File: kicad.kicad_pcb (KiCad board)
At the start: 2 copper layers, 0 parts

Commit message: demasiados cambios mi loco
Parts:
- added C1: 100nF, Capacitor_SMD:C_1206_3216Metric_Pad1.33x1.80mm_HandSolder, F.Cu at (121.9, 113.0)
- added C10: 470uF, libs:CAP_10x10_SMD_THT, F.Cu at (116.8, 88.4)
- added C11: 470uF, libs:CAP_10x10_SMD_THT, F.Cu at (133.8, 64.2)
- added C12: 470uF, libs:CAP_10x10_SMD_THT, F.Cu at (116.8, 76.6)
- added C18: 100nF, Capacitor_SMD:C_1206_3216Metric_Pad1.33x1.80mm_HandSolder, F.Cu at (166.3, 102.7)
- added C19: 100nF, Capacitor_SMD:C_1206_3216Metric_Pad1.33x1.80mm_HandSolder, F.Cu at (166.3, 99.3)
- added C22: 1uF, Capacitor_SMD:C_1206_3216Metric_Pad1.33x1.80mm_HandSolder, F.Cu at (107.8, 126.0)
- added C5: 470uF, libs:CAP_10x10_SMD_THT, F.Cu at (130.9, 87.9)
- added C6: 470uF, libs:CAP_10x10_SMD_THT, F.Cu at (119.8, 64.2)
- added C7: 100nF, Capacitor_SMD:C_1206_3216Metric_Pad1.33x1.80mm_HandSolder, F.Cu at (140.7, 84.6)
- added C8: 470uF, libs:CAP_10x10_SMD_THT, F.Cu at (147.9, 64.2)
- added C9: 470uF, libs:CAP_10x10_SMD_THT, F.Cu at (130.9, 76.1)
- added D15: BAT54S, Package_TO_SOT_SMD:SOT-23, F.Cu at (205.4, 60.6)
- added D2: SS14, Diode_SMD:D_SMA_Handsoldering, F.Cu at (99.8, 126.7)
- added D5: LED, LED_SMD:LED_1206_3216Metric, F.Cu at (186.4, 64.5)
- added D6: LED, LED_SMD:LED_1206_3216Metric, F.Cu at (150.4, 78.3)
- added D7: SS14, Diode_SMD:D_SMA_Handsoldering, F.Cu at (142.7, 72.4)
- added D8: M7, Diode_SMD:D_SMA_Handsoldering, F.Cu at (188.6, 60.6)
- added D9: BAT54S, Package_TO_SOT_SMD:SOT-23, F.Cu at (170.2, 81.7)
- added J1: Screw_Terminal_01x02, libs:TerminalBlock_bornier-2_P5.08mm, F.Cu at (138.8, 102.2)
- added J2: Screw_Terminal_01x03, libs:TerminalBlock_bornier-3_P5.08mm, F.Cu at (122.2, 102.2)
- added J3: ICSP, Connector_PinSocket_2.54mm:PinSocket_1x06_P2.54mm_Vertical, F.Cu at (116.6, 100.0)
- added J4: Conn_01x05, Connector_Molex:Molex_KK-254_AE-6410-05A_1x05_P2.54mm_Vertical, F.Cu at (116.6, 118.9)
- added J7: Conn_01x03, Connector_Molex:Molex_KK-254_AE-6410-03A_1x03_P2.54mm_Vertical, F.Cu at (155.9, 101.6)
- added JP1: SolderJumper_2_Open, Jumper:SolderJumper-2_P1.3mm_Open_RoundedPad1.0x1.5mm, F.Cu at (156.9, 60.1)
- added K1: RELAY, Relay_THT:Relay_SPDT_SANYOU_SRD_Series_Form_C, F.Cu at (164.5, 66.8)
- added L1: 68uH, libs:L_12x12mm_H8mm, F.Cu at (102.2, 77.8)
- added Q1: BC817, Package_TO_SOT_SMD:SOT-23, F.Cu at (191.4, 65.1)
- added R1: 10k, Resistor_SMD:R_1206_3216Metric, F.Cu at (142.4, 118.2)
- added R11: 10k, Resistor_SMD:R_1206_3216Metric, F.Cu at (142.4, 111.6)
- added R12: 10k, Resistor_SMD:R_1206_3216Metric, F.Cu at (129.7, 125.5)
- added R15: 10k, Resistor_SMD:R_1206_3216Metric, F.Cu at (142.4, 108.3)
- added R16: 1k, Resistor_SMD:R_1206_3216Metric, F.Cu at (103.2, 93.0)
- added R17: 330, Resistor_SMD:R_1206_3216Metric, F.Cu at (97.6, 93.0)
- added R18: 1k, Resistor_SMD:R_1206_3216Metric, F.Cu at (165.2, 84.3)
- added R19: 1k, Resistor_SMD:R_1206_3216Metric, F.Cu at (165.2, 81.0)
- added R2: 10k, Resistor_SMD:R_1206_3216Metric, F.Cu at (135.3, 125.5)
- added R20: 10k, Resistor_SMD:R_1206_3216Metric, F.Cu at (142.4, 121.5)
- added R23: 1k, Resistor_SMD:R_1206_3216Metric, F.Cu at (200.4, 59.9)
- added R24: 1k, Resistor_SMD:R_1206_3216Metric, F.Cu at (200.4, 63.2)
- added R3: 1k, Resistor_SMD:R_1206_3216Metric, F.Cu at (186.4, 71.2)
- added R4: 1k, Resistor_SMD:R_1206_3216Metric, F.Cu at (186.4, 67.9)
- added R5: 22k, Resistor_SMD:R_1206_3216Metric, F.Cu at (124.1, 124.5)
- added R6: 5k6, Resistor_SMD:R_1206_3216Metric, F.Cu at (142.4, 114.9)
- added RV1: 10k, Potentiometer_THT:Potentiometer_Bourns_3296W_Vertical, F.Cu at (102.9, 88.1)
- added SW1: SW_Push, Button_Switch_THT:SW_PUSH_6mm, F.Cu at (131.1, 117.3)
- added SW2: SW_Push, Button_Switch_THT:SW_PUSH_6mm, F.Cu at (131.1, 108.7)
- added U1: ADS1115IDGS, Package_SO:TSSOP-10_3x3mm_P0.5mm, F.Cu at (117.8, 125.1)
- added U2: ESP-12E, ESP8266:ESP-12E_SMD, F.Cu at (97.5, 106.9)
- added U3: ADS1115IDGS, Package_SO:TSSOP-10_3x3mm_P0.5mm, F.Cu at (122.4, 109.0)
- added U4: KF33BD-TR, Package_SO:SO-8_3.9x4.9mm_P1.27mm, F.Cu at (152.0, 73.4)
- added U7: LM2596S-3.3, libs:TO-263-5_TabPin3, F.Cu at (103.6, 64.5)
- added U9: AMS1117-5.0, Package_TO_SOT_SMD:SOT-223-3_TabPin2, F.Cu at (142.6, 78.8)

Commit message: quiero dormir culiaaaa
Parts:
- removed C10, C11, C12: 470uF, libs:CAP_10x10_SMD_THT
- removed C18, C19: 100nF, Capacitor_SMD:C_1206_3216Metric_Pad1.33x1.80mm_HandSolder
- removed C22: 1uF, Capacitor_SMD:C_1206_3216Metric_Pad1.33x1.80mm_HandSolder
- removed D15, D9: BAT54S, Package_TO_SOT_SMD:SOT-23
- removed D6: LED, LED_SMD:LED_1206_3216Metric
- removed D7: SS14, Diode_SMD:D_SMA_Handsoldering
- removed D8: M7, Diode_SMD:D_SMA_Handsoldering
- removed JP1: SolderJumper_2_Open, Jumper:SolderJumper-2_P1.3mm_Open_RoundedPad1.0x1.5mm
- removed L1: 68uH, libs:L_12x12mm_H8mm
- removed R18, R19, R23, R24: 1k, Resistor_SMD:R_1206_3216Metric
- removed R20: 10k, Resistor_SMD:R_1206_3216Metric
- removed RV1: 10k, Potentiometer_THT:Potentiometer_Bourns_3296W_Vertical
- removed U4: KF33BD-TR, Package_SO:SO-8_3.9x4.9mm_P1.27mm
- removed U7: LM2596S-3.3, libs:TO-263-5_TabPin3
- removed U9: AMS1117-5.0, Package_TO_SOT_SMD:SOT-223-3_TabPin2
- added C2: 100nF, Capacitor_SMD:C_1206_3216Metric_Pad1.33x1.80mm_HandSolder, F.Cu at (172.9, 67.8)
- added C3: 1uF, Capacitor_SMD:C_1206_3216Metric_Pad1.33x1.80mm_HandSolder, F.Cu at (145.7, 101.6)
- added C4: 100nF, Capacitor_SMD:C_1206_3216Metric_Pad1.33x1.80mm_HandSolder, F.Cu at (180.0, 71.1)
- added D1: LED, LED_SMD:LED_1206_3216Metric, F.Cu at (189.4, 54.2)
- added D3: LED, LED_SMD:LED_1206_3216Metric, F.Cu at (145.6, 105.0)
- added D4: M7, Diode_SMD:D_SMA_Handsoldering, F.Cu at (175.0, 63.8)
- added J5: Conn_01x03, Connector_Molex:Molex_KK-254_AE-6410-03A_1x03_P2.54mm_Vertical, F.Cu at (182.3, 65.5)
- added J6: ICSP, Connector_PinSocket_2.54mm:PinSocket_1x06_P2.54mm_Vertical, F.Cu at (134.7, 73.1)
- added J8: Screw_Terminal_01x03, libs:TerminalBlock_bornier-3_P5.08mm, F.Cu at (173.2, 57.0)
- added K2: RELAY 0510, Relay_THT:Relay_SPDT_SANYOU_SRD_Series_Form_C, F.Cu at (113.3, 82.5)
- added PS1: HLK-PM01, Converter_ACDC:Converter_ACDC_HiLink_HLK-PMxx, F.Cu at (95.0, 60.8)
- added Q2: BC817, Package_TO_SOT_SMD:SOT-23, F.Cu at (185.2, 75.0)
- added R10: 10k, Resistor_SMD:R_1206_3216Metric, F.Cu at (173.9, 83.4)
- added R13: 220, Resistor_SMD:R_1206_3216Metric, F.Cu at (151.2, 107.1)
- added R14: 1k, Resistor_SMD:R_1206_3216Metric, F.Cu at (157.2, 101.9)
- added R7: 1k, Resistor_SMD:R_1206_3216Metric, F.Cu at (159.8, 92.0)
- added R8: ?, Resistor_SMD:R_1206_3216Metric, F.Cu at (151.6, 100.5)
- added R9: 220, Resistor_SMD:R_1206_3216Metric, F.Cu at (179.8, 77.7)
- added T1: ZMPT101B, ZMPT101B:ZMPT101B, F.Cu at (138.4, 61.6)
- C1: value 100nF -> 470uF; footprint Capacitor_SMD:C_1206_3216Metric_Pad1.33x1.80mm_HandSolder -> libs:CAP_10x10_SMD_THT
- C6, C8: value 470uF -> 100nF; footprint libs:CAP_10x10_SMD_THT -> Capacitor_SMD:C_1206_3216Metric_Pad1.33x1.80mm_HandSolder
- C9: value 470uF -> 1uF; footprint libs:CAP_10x10_SMD_THT -> Capacitor_SMD:C_1206_3216Metric_Pad1.33x1.80mm_HandSolder
- D2: value SS14 -> LED; footprint Diode_SMD:D_SMA_Handsoldering -> LED_SMD:LED_1206_3216Metric
- D5: value LED -> M7; footprint LED_SMD:LED_1206_3216Metric -> Diode_SMD:D_SMA_Handsoldering
- J2: value Screw_Terminal_01x03 -> jack3.5mm; footprint libs:TerminalBlock_bornier-3_P5.08mm -> Connector_Audio:Jack_3.5mm_Ledino_KB3SPRS_Horizontal
- J3: value ICSP -> Screw_Terminal_01x02; footprint Connector_PinSocket_2.54mm:PinSocket_1x06_P2.54mm_Vertical -> libs:TerminalBlock_bornier-2_P5.08mm
- J7: value Conn_01x03 -> Screw_Terminal_01x03; footprint Connector_Molex:Molex_KK-254_AE-6410-03A_1x03_P2.54mm_Vertical -> libs:TerminalBlock_bornier-3_P5.08mm
- K1: value RELAY -> RELAY 0510
- R1, R2: value 10k -> 100k
- R12: value 10k -> 220
- R15: value 10k -> 1k
- R16, R3, R4: value 1k -> 10k
- R17: value 330 -> 10k
- R5: value 22k -> 10k
- R6: value 5k6 -> 10k
- U1: value ADS1115IDGS -> KF33BD-TR; footprint Package_SO:TSSOP-10_3x3mm_P0.5mm -> Package_SO:SO-8_3.9x4.9mm_P1.27mm
- U2: value ESP-12E -> ADS1015IDGS; footprint ESP8266:ESP-12E_SMD -> Package_SO:TSSOP-10_3x3mm_P0.5mm
- U3: value ADS1115IDGS -> ESP-12E; footprint Package_SO:TSSOP-10_3x3mm_P0.5mm -> ESP8266:ESP-12E_SMD
- moved D2 113.2 mm to (189.4, 57.6)
- moved Q1 91.0 mm to (108.7, 103.0)
- moved R17 82.8 mm to (179.5, 81.0)
- moved R2 74.2 mm to (185.8, 71.0)
- moved R16 71.9 mm to (173.9, 80.2)
- moved J3 58.2 mm to (168.7, 74.0)
- moved C8 53.9 mm to (115.5, 107.2)
- moved U1 52.2 mm to (141.2, 78.5)
- moved U2 48.6 mm to (140.5, 84.1)
- moved D5 45.2 mm to (142.0, 73.0)
- moved C6 43.7 mm to (127.5, 107.2)
- moved SW2 42.3 mm to (162.6, 80.5)
- moved R12 40.4 mm to (159.8, 98.6)
- moved R1 39.7 mm to (169.0, 88.7)
- moved R4 38.1 mm to (159.8, 95.3)
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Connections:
- C1 pad 1: +3V3 -> +5V
- C5 pad 1: +12V -> +3V3
- C6 pad 1: +12V -> +3V3
- C7 pad 1: +12V -> +3V3
- C8 pad 1: +12V -> +3V3
- C9 pad 1: +5V -> +3V3
- D2 pad 1: +12V -> Net-(D2-Pad1)
- D2 pad 2: +BATT -> +5V
- D5 pad 1: Net-(D5-Pad1) -> +5V
- D5 pad 2: +12V -> Net-(D5-Pad2)
- J1 pad 1: +BATT -> Net-(J1-Pad1)
- J1 pad 2: GND -> Net-(J1-Pad2)
- J3 pad 1: RESET -> Net-(J2-PadS)
- J3 pad 2: TXD0 -> Net-(J2-PadT)
- J7 pad 1: +3V3 -> Net-(J7-Pad1)
- J7 pad 2: /Prot LM35/IN -> Net-(J7-Pad2)
- J7 pad 3: GND -> Net-(J7-Pad3)
- K1 pad 1: /Relay 1/COM -> Net-(J7-Pad2)
- K1 pad 2: Net-(D8-Pad2) -> Net-(D4-Pad2)
- K1 pad 3: /Relay 1/NO -> Net-(J7-Pad1)
- K1 pad 4: /Relay 1/NC -> Net-(J7-Pad3)
- K1 pad 5: +12V -> +5V
- Q1 pad 3: Net-(D8-Pad2) -> Net-(D4-Pad2)
- R1 pad 1: +3V3 -> Net-(R1-Pad1)
- R1 pad 2: RESET -> Net-(J1-Pad1)
- R11 pad 1: +3V3 -> Net-(J2-PadT)
- R11 pad 2: SDA -> GND
- R12 pad 1: +3V3 -> Net-(D2-Pad1)
- R12 pad 2: SCL -> Net-(D4-Pad2)
- R15 pad 1: +3V3 -> Net-(Q2-Pad1)
- R15 pad 2: Net-(R15-Pad2) -> RELAY_2
- R16 pad 1: Net-(D6-Pad1) -> +3V3
- R16 pad 2: GND -> Net-(R16-Pad2)
- R2 pad 1: +3V3 -> Net-(R2-Pad1)
- R2 pad 2: GPIO0 -> Net-(R1-Pad1)
- R3 pad 1: Net-(D5-Pad1) -> +3V3
- R3 pad 2: Net-(D8-Pad2) -> SDA
- R4 pad 1: Net-(Q1-Pad1) -> +3V3
- R4 pad 2: RELAY_1 -> SCL
- R5 pad 1: +12V -> +3V3
- R5 pad 2: /Input Protection/IN -> RESET
- R6 pad 1: /Input Protection/IN -> +3V3
- R6 pad 2: GND -> GPIO0
- U1 pad 1: GND -> +3V3
- U1 pad 2: RDY1 -> GND
- U1 pad 5: Net-(U1-Pad5) -> GND
- U1 pad 6: Net-(U1-Pad6) -> GND
- U1 pad 7: Net-(U1-Pad7) -> GND
- U1 pad 8: +3V3 -> +5V
- U2 pad 1: RESET -> GND
- U2 pad 10: Net-(R20-Pad1) -> SCL
- U2 pad 2: TEMP -> RDY
- U2 pad 3: +3V3 -> GND
- U2 pad 4: RESET -> Net-(C3-Pad2)
- U2 pad 5: RELAY_1 -> Net-(J2-PadS)
- U2 pad 6: RDY1 -> Net-(U2-Pad6)
- U2 pad 7: RDY2 -> Net-(J2-PadT)
- U2 pad 9: GND -> SDA
- U3 pad 1: +3V3 -> RESET
- U3 pad 10: SCL -> Net-(R17-Pad1)
- U3 pad 2: RDY1 -> TEMP
- U3 pad 3: GND -> +3V3
- U3 pad 4: Net-(U3-Pad4) -> RESET
- U3 pad 5: Net-(U3-Pad5) -> RELAY_1
- U3 pad 6: Net-(U3-Pad6) -> RELAY_2
- U3 pad 7: Net-(U3-Pad7) -> RDY
- U3 pad 9: SDA -> GND

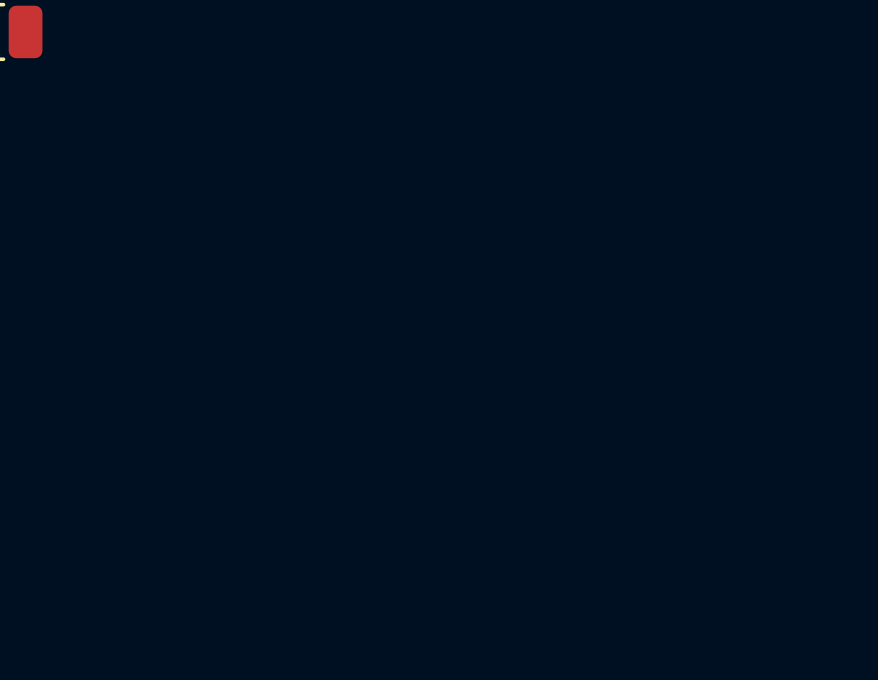
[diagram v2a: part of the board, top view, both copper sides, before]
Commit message: Esquematico final del proyecto.
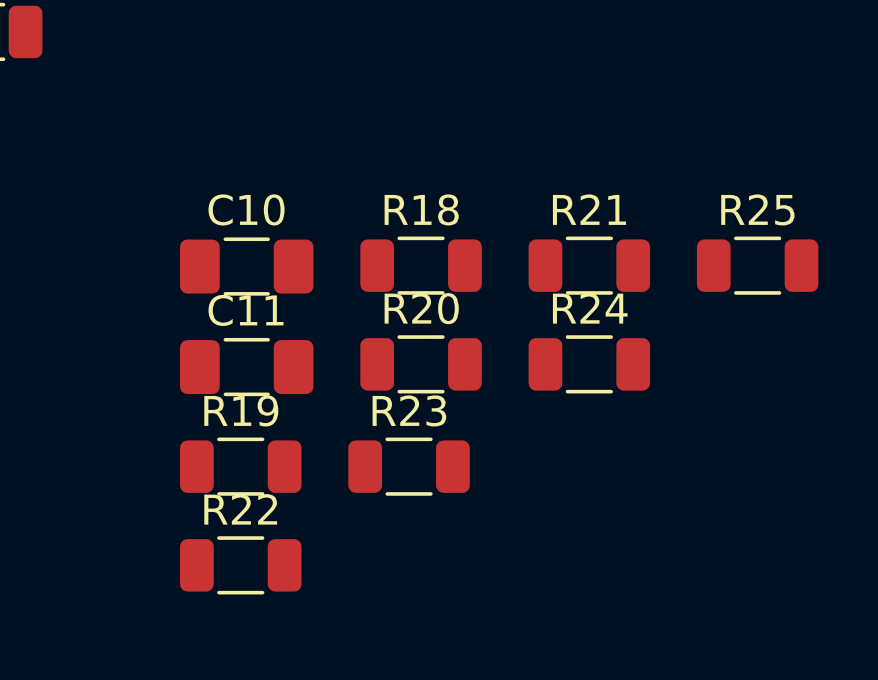
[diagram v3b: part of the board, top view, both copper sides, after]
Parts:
- added C10: 100nF, Capacitor_SMD:C_1206_3216Metric_Pad1.33x1.80mm_HandSolder, F.Cu at (177.8, 96.5)
- added C11: 1uF, Capacitor_SMD:C_1206_3216Metric_Pad1.33x1.80mm_HandSolder, F.Cu at (177.8, 99.9)
- added R18: 10k, Resistor_SMD:R_1206_3216Metric, F.Cu at (183.6, 96.5)
- added R19: 10k, Resistor_SMD:R_1206_3216Metric, F.Cu at (177.6, 103.2)
- added R20: 220, Resistor_SMD:R_1206_3216Metric, F.Cu at (183.6, 99.8)
- added R21: 220, Resistor_SMD:R_1206_3216Metric, F.Cu at (189.2, 96.5)
- added R22: 1k, Resistor_SMD:R_1206_3216Metric, F.Cu at (177.6, 106.5)
- added R23: 1k, Resistor_SMD:R_1206_3216Metric, F.Cu at (183.2, 103.2)
- added R24: 10k, Resistor_SMD:R_1206_3216Metric, F.Cu at (189.2, 99.8)
- added R25: 10k, Resistor_SMD:R_1206_3216Metric, F.Cu at (194.8, 96.5)
- C1, C5: value 470uF -> 100nF
- C3: value 1uF -> 470uF
- C8: value 100nF -> 470uF
- C9: value 1uF -> 100nF
- J1: value Screw_Terminal_01x02 -> Conn_01x03
- J2: value jack3.5mm -> Screw_Terminal_01x02
- J3: value Screw_Terminal_01x02 -> Conn_01x05
- J4: value Conn_01x05 -> jack3.5mm
- J5: value Conn_01x03 -> Screw_Terminal_01x02
- R1, R2: value 100k -> 10k
- R10, R11: value 10k -> 27k
- R12, R13: value 220 -> 1k
- R14: value 1k -> 220
- R15, R7: value 1k -> 470
- R16, R6: value 10k -> 470
- R3: value 10k -> 220k
- R4: value 10k -> 1k
- R5: value 10k -> ?
- R8: value ? -> 10k
- R9: value 220 -> 10k
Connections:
- C1 pad 1: +5V -> TEMP
- C2 pad 1: +5V -> +3V3
- C3 pad 1: Net-(C3-Pad1) -> +5V
- C3 pad 2: Net-(C3-Pad2) -> GND
- C4 pad 1: TEMP -> Net-(C4-Pad1)
- C5 pad 1: +3V3 -> Net-(C5-Pad1)
- C6 pad 1: +3V3 -> +5V
- C7 pad 1: +3V3 -> Net-(C7-Pad1)
- J1 pad 1: Net-(J1-Pad1) -> +3V3
- J1 pad 2: Net-(J1-Pad2) -> TEMP
- J2 pad R: Net-(J2-PadR) -> (no net)
- J2 pad S: Net-(J2-PadS) -> (no net)
- J2 pad T: Net-(J2-PadT) -> (no net)
- J3 pad 1: Net-(J2-PadS) -> SCL
- J3 pad 2: Net-(J2-PadT) -> SDA
- J4 pad 1: SCL -> (no net)
- J4 pad 2: SDA -> (no net)
- J4 pad 3: +3V3 -> (no net)
- J4 pad 4: +5V -> (no net)
- J4 pad 5: GND -> (no net)
- J5 pad 1: +3V3 -> Net-(J4-PadS)
- J5 pad 2: TEMP -> Net-(C7-Pad1)
- J5 pad 3: GND -> (no net)
- J6 pad 2: TXD0 -> Net-(J6-Pad2)
- J6 pad 3: RXD0 -> Net-(J6-Pad3)
- PS1 pad 1: Net-(J1-Pad1) -> Net-(J2-Pad2)
- PS1 pad 2: Net-(J1-Pad2) -> Net-(J2-Pad1)
- R1 pad 1: Net-(R1-Pad1) -> +3V3
- R1 pad 2: Net-(J1-Pad1) -> SDA
- R10 pad 1: +3V3 -> Net-(C4-Pad1)
- R10 pad 2: Net-(J2-PadT) -> Net-(R10-Pad2)
- R11 pad 1: Net-(J2-PadT) -> Net-(C5-Pad1)
- R11 pad 2: GND -> Net-(J4-PadS)
- R12 pad 1: Net-(D2-Pad1) -> Net-(R12-Pad1)
- R12 pad 2: Net-(D4-Pad2) -> Net-(C4-Pad1)
- R13 pad 1: Net-(D3-Pad1) -> Net-(R13-Pad1)
- R13 pad 2: Net-(D5-Pad2) -> Net-(C5-Pad1)
- R14 pad 1: Net-(Q1-Pad1) -> Net-(D1-Pad1)
- R14 pad 2: RELAY_1 -> GND
- R15 pad 1: Net-(Q2-Pad1) -> TXD0
- R15 pad 2: RELAY_2 -> Net-(J6-Pad2)
- R16 pad 1: +3V3 -> RXD0
- R16 pad 2: Net-(R16-Pad2) -> Net-(J6-Pad3)
- R17 pad 1: Net-(R17-Pad1) -> +3V3
- R17 pad 2: GND -> RDY
- R2 pad 1: Net-(R2-Pad1) -> +3V3
- R2 pad 2: Net-(R1-Pad1) -> SCL
- R3 pad 1: +3V3 -> Net-(R3-Pad1)
- R3 pad 2: SDA -> Net-(J2-Pad1)
- R4 pad 1: +3V3 -> Net-(C7-Pad1)
- R4 pad 2: SCL -> Net-(R10-Pad2)
- R5 pad 1: +3V3 -> Net-(J4-PadS)
- R5 pad 2: RESET -> Net-(C7-Pad1)
- R6 pad 1: +3V3 -> RESET
- R6 pad 2: GPIO0 -> Net-(R6-Pad2)
- R7 pad 1: Net-(J2-PadT) -> GPIO0
- R7 pad 2: Net-(C3-Pad1) -> Net-(R7-Pad2)
- R8 pad 1: Net-(J2-PadS) -> +3V3
- R8 pad 2: Net-(J2-PadT) -> RESET
- R9 pad 1: Net-(D1-Pad1) -> +3V3
- R9 pad 2: GND -> GPIO0
- SW1 pad 2: RESET -> Net-(R6-Pad2)
- SW2 pad 2: GPIO0 -> Net-(R7-Pad2)
- T1 pad 1: Net-(R2-Pad1) -> Net-(R3-Pad1)
- T1 pad 2: Net-(J1-Pad2) -> Net-(J2-Pad2)
- T1 pad 3: Net-(C3-Pad1) -> Net-(R10-Pad2)
- T1 pad 4: Net-(J2-PadT) -> Net-(C7-Pad1)
- U2 pad 4: Net-(C3-Pad2) -> Net-(R12-Pad1)
- U2 pad 5: Net-(J2-PadS) -> Net-(R13-Pad1)
- U2 pad 7: Net-(J2-PadT) -> Net-(C7-Pad1)
- U3 pad 10: Net-(R17-Pad1) -> Net-(R25-Pad1)
- U3 pad 11: Net-(R16-Pad2) -> Net-(R24-Pad2)

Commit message: Diseño de pcb arrancado
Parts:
- C1, C5: footprint libs:CAP_10x10_SMD_THT -> Capacitor_SMD:C_1206_3216Metric_Pad1.33x1.80mm_HandSolder
- C3, C8: footprint Capacitor_SMD:C_1206_3216Metric_Pad1.33x1.80mm_HandSolder -> libs:CAP_10x10_SMD_THT
- J1: footprint libs:TerminalBlock_bornier-2_P5.08mm -> Connector_Molex:Molex_KK-254_AE-6410-03A_1x03_P2.54mm_Vertical
- J2: footprint Connector_Audio:Jack_3.5mm_Ledino_KB3SPRS_Horizontal -> libs:TerminalBlock_bornier-2_P5.08mm
- J3: footprint libs:TerminalBlock_bornier-2_P5.08mm -> Connector_Molex:Molex_KK-254_AE-6410-05A_1x05_P2.54mm_Vertical
- J4: footprint Connector_Molex:Molex_KK-254_AE-6410-05A_1x05_P2.54mm_Vertical -> Connector_Audio:Jack_3.5mm_Ledino_KB3SPRS_Horizontal
- J5: footprint Connector_Molex:Molex_KK-254_AE-6410-03A_1x03_P2.54mm_Vertical -> libs:TerminalBlock_bornier-2_P5.08mm
- moved J5 77.4 mm to (126.1, 118.7), turned to 270 degrees
- moved J8 73.4 mm to (193.4, 127.6), turned to 90 degrees
- moved R3 70.0 mm to (113.6, 97.2), turned to 180 degrees
- moved K2 69.3 mm to (169.9, 122.6)
- moved J1 69.2 mm to (194.0, 69.2), turned to 270 degrees
- moved U3 68.2 mm to (162.3, 76.2)
- moved J7 55.2 mm to (193.4, 110.5), turned to 90 degrees
- moved Q2 55.1 mm to (162.3, 125.1)
- moved D5 55.1 mm to (166.1, 122.6), turned to 270 degrees
- moved C4 54.1 mm to (141.6, 109.2), turned to 180 degrees
- moved Q1 53.8 mm to (162.3, 108.0)
- moved SW2 53.1 mm to (133.6, 125.0)
- moved R9 50.7 mm to (157.8, 123.4), turned to 270 degrees
- moved C1 50.4 mm to (185.5, 73.0), turned to 180 degrees
- moved K1 48.3 mm to (169.9, 105.4)
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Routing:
- net Net-(J2-Pad2): track 0.00 -> 56.3 mm
- net +5V: track 0.00 -> 36.4 mm
- net Net-(J2-Pad1): track 0.00 -> 30.3 mm
- net Net-(J8-Pad2): track 0.00 -> 23.5 mm
- net Net-(J7-Pad2): track 0.00 -> 23.5 mm
- net Net-(J4-PadS): track 0.00 -> 22.9 mm
- net Net-(C7-Pad1): track 0.00 -> 17.0 mm
- net +3V3: track 0.00 -> 12.9 mm
- net Net-(J7-Pad1): track 0.00 -> 9.75 mm
- net Net-(J8-Pad1): track 0.00 -> 9.75 mm
- net Net-(J7-Pad3): track 0.00 -> 9.68 mm
- net Net-(J8-Pad3): track 0.00 -> 9.68 mm
- net GND: track 0.00 -> 8.90 mm
- net Net-(R3-Pad1): track 0.00 -> 7.84 mm
- net Net-(C5-Pad1): track 0.00 -> 7.12 mm
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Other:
- board outline added: 100 x 70 mm
- net class Default: clearance 0.2 -> 0.31; trace_width 0.25 -> 0.31; via_drill 0.4 -> 0.45
- net class HiPower added: clearance 0.31, trace_width 0.6, via_dia 1.6, via_drill 0.75
- net class Power added: clearance 0.31, trace_width 0.6, via_dia 0.8, via_drill 0.45
- rule trace_clearance: 0.2 -> 0.31
- rule trace_min: 0.2 -> 0.31
- rule via_min_drill: 0.3 -> 0.45
- rule via_min_size: 0.4 -> 0.6

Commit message: algo ruteado
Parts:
- moved C10 1.18 mm to (151.1, 95.0)
- moved C11 1.18 mm to (153.7, 95.0)
- moved R23 0.47 mm to (158.1, 97.6)
- moved R22 0.39 mm to (161.0, 97.6)
- turned R21 to 270 degrees
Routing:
- net Net-(C7-Pad1): track 17.0 -> 105.4 mm
- net +3V3: track 12.9 -> 89.5 mm
- net Net-(Q2-Pad1): track 0.00 -> 26.1 mm
- net Net-(R7-Pad2): track 0.00 -> 26.1 mm
- net +5V: track 36.4 -> 56.0 mm
- net RESET: track 0.00 -> 18.5 mm
- net GPIO0: track 0.00 -> 16.6 mm
- net Net-(J4-PadS): track 22.9 -> 37.7 mm
- net Net-(D4-Pad2): track 0.00 -> 13.9 mm
- net Net-(D5-Pad2): track 0.00 -> 13.9 mm
- net Net-(R10-Pad2): track 3.81 -> 13.9 mm
- net Net-(R6-Pad2): track 0.00 -> 9.94 mm
- net Net-(Q1-Pad1): track 0.00 -> 8.13 mm
- net TXD0: track 0.00 -> 8.10 mm
- net Net-(R24-Pad2): track 0.00 -> 8.04 mm
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- added copper zone on B.Cu, net GND
- added copper zone on F.Cu, net GND
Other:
- net class Default: clearance 0.31 -> 0.15
- net class HiPower: clearance 0.31 -> 0.15
- net class Power: clearance 0.31 -> 0.15
- rule trace_clearance: 0.31 -> 0.15
